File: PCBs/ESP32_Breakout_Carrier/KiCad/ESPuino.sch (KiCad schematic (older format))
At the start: 15 parts, among them J1 SD-Card Reader, J2 RFID-RC522, J3 Adafruit MAX98357, J4 Rotary Encode, J5 Next, J6 Prev, J7 Pause, J8 WS2812, J9 Power, Q1 BC337, Q2 IRF9540N, U1 ESP32-DEVKITC-32U

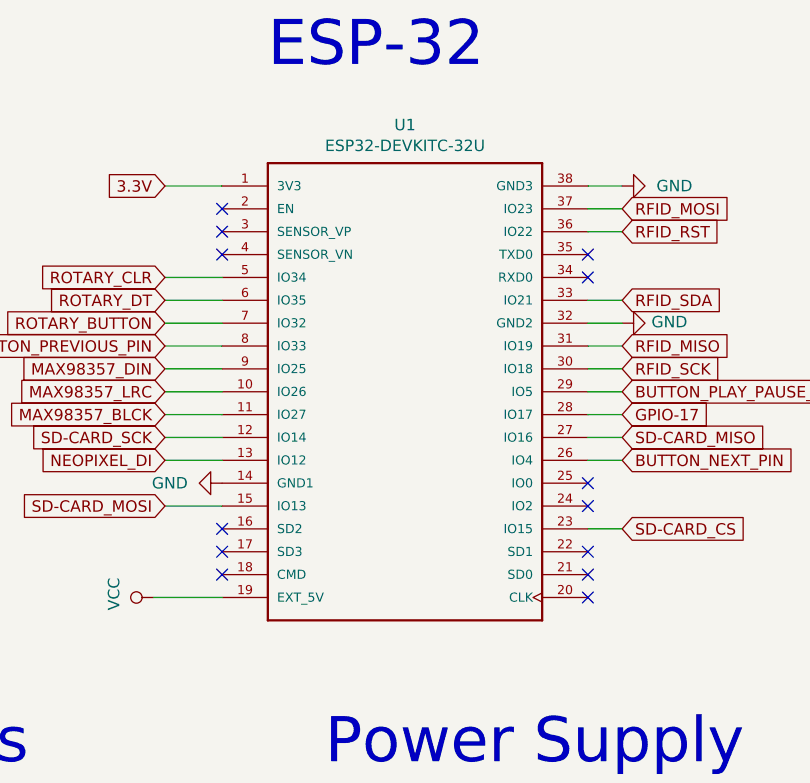
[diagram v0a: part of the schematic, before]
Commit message: use snapEDA footprint and create 3d-model for ESP32_Breakout_Carrier
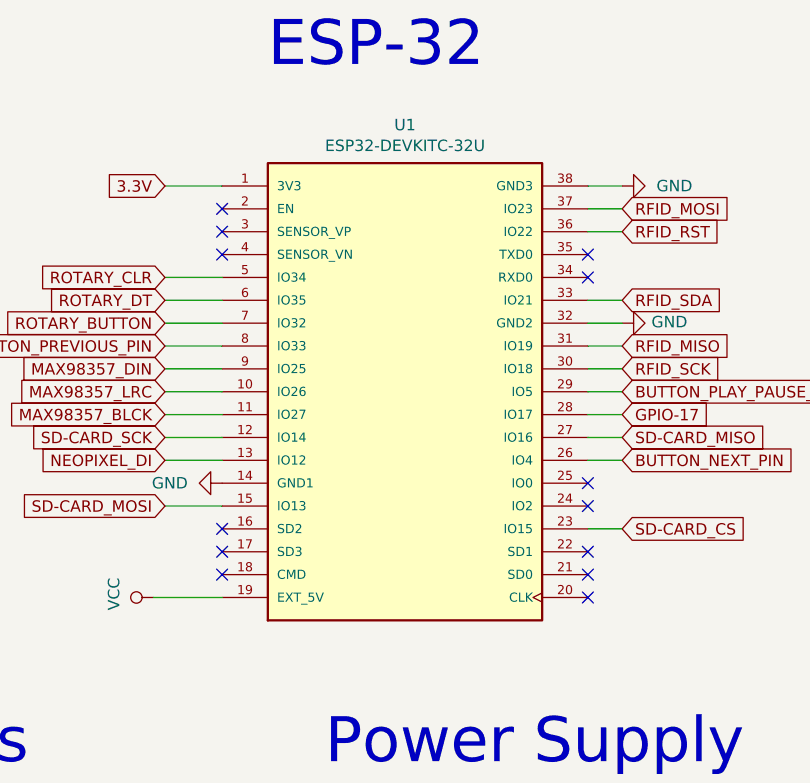
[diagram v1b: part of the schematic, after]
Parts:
- removed U1: ESP32-DEVKITC-32U, ESP32_Breakout_Carrier:MODULE_ESP32-DEVKITC-32U, symbol ESPuino-rescue:ESP32-DEVKITC-32U-ESP32-DEVKITC-32U
- added U1: ESP32-DEVKITC-32U, ESPuino_snapEDA:MODULE_ESP32-DEVKITC-32U, symbol ESPuino_snapEDA:ESP32-DEVKITC-32U
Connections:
- net 3.3V: now also U1.1 (3V3)
- net BUTTON_NEXT_PIN: now also U1.26 (IO4)
- net BUTTON_PLAY_PAUSE_PIN: now also U1.29 (IO5)
- net BUTTON_PREVIOUS_PIN: now also U1.8 (IO33)
- net GND: now also U1.14 (GND1), U1.32 (GND2), U1.38 (GND3)
- net GPIO-17: now also U1.28 (IO17)
- net MAX98357_BLCK: now also U1.11 (IO27)
- net MAX98357_DIN: now also U1.9 (IO25)
- net MAX98357_LRC: now also U1.10 (IO26)
- net NEOPIXEL_DI: now also U1.13 (IO12)
- net RFID_MISO: now also U1.31 (IO19)
- net RFID_MOSI: now also U1.37 (IO23)
- net RFID_RST: now also U1.36 (IO22)
- net RFID_SCK: now also U1.30 (IO18)
- net RFID_SDA: now also U1.33 (IO21)
- net ROTARY_BUTTON: now also U1.7 (IO32)
- net ROTARY_CLR: now also U1.5 (IO34)
- net ROTARY_DT: now also U1.6 (IO35)
- net SD-CARD_CS: now also U1.23 (IO15)
- net SD-CARD_MISO: now also U1.27 (IO16)
- net SD-CARD_MOSI: now also U1.15 (IO13)
- net SD-CARD_SCK: now also U1.12 (IO14)
- net VCC: now also U1.19 (EXT_5V)
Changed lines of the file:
@@
 $EndDescr
-$Comp
-L ESPuino-rescue:ESP32-DEVKITC-32U-ESP32-DEVKITC-32U U1
-U 1 1 5F79096D
-P 8100 2650
-F 0 "U1" H 8100 3817 50  0000 C CNN
-F 1 "ESP32-DEVKITC-32U" H 8100 3726 50  0000 C CNN
-F 2 "ESP32_Breakout_Carrier:MODULE_ESP32-DEVKITC-32U" H 8100 2650 50  0001 L BNN
-F 3 "Manufacturer Recommendations" H 8100 2650 50  0001 L BNN
-F 4 "ESPRESSIF" H 8100 2650 50  0001 L BNN "Field4"
-F 5 "N/A" H 8100 2650 50  0001 L BNN "Field5"
-	1    8100 2650
-	1    0    0    -1
-$EndComp
 $Comp
 L Connector:Conn_01x05_Male J4
@@
 NoConn ~ 4650 6650
 NoConn ~ 4750 5250
+$Comp
+L ESPuino_snapEDA:ESP32-DEVKITC-32U U1
+U 1 1 6028D38A
+P 8100 2650
+F 0 "U1" H 8100 3817 50  0000 C CNN
+F 1 "ESP32-DEVKITC-32U" H 8100 3726 50  0000 C CNN
+F 2 "ESPuino_snapEDA:MODULE_ESP32-DEVKITC-32U" H 8100 2650 50  0001 L BNN
+F 3 "" H 8100 2650 50  0001 L BNN
+F 4 "Manufacturer Recommendations" H 8100 2650 50  0001 L BNN "STANDARD"
+F 5 "N/A" H 8100 2650 50  0001 L BNN "PARTREV"
+F 6 "ESPRESSIF" H 8100 2650 50  0001 L BNN "MANUFACTURER"
+	1    8100 2650
+	1    0    0    -1
+$EndComp
 $EndSCHEMATC
